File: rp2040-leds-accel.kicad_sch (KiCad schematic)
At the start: 9 parts, among them J1 USB_C_Receptacle_USB2.0_16P, U1 AMS1117-3.3, U2 AMS1117-5.0

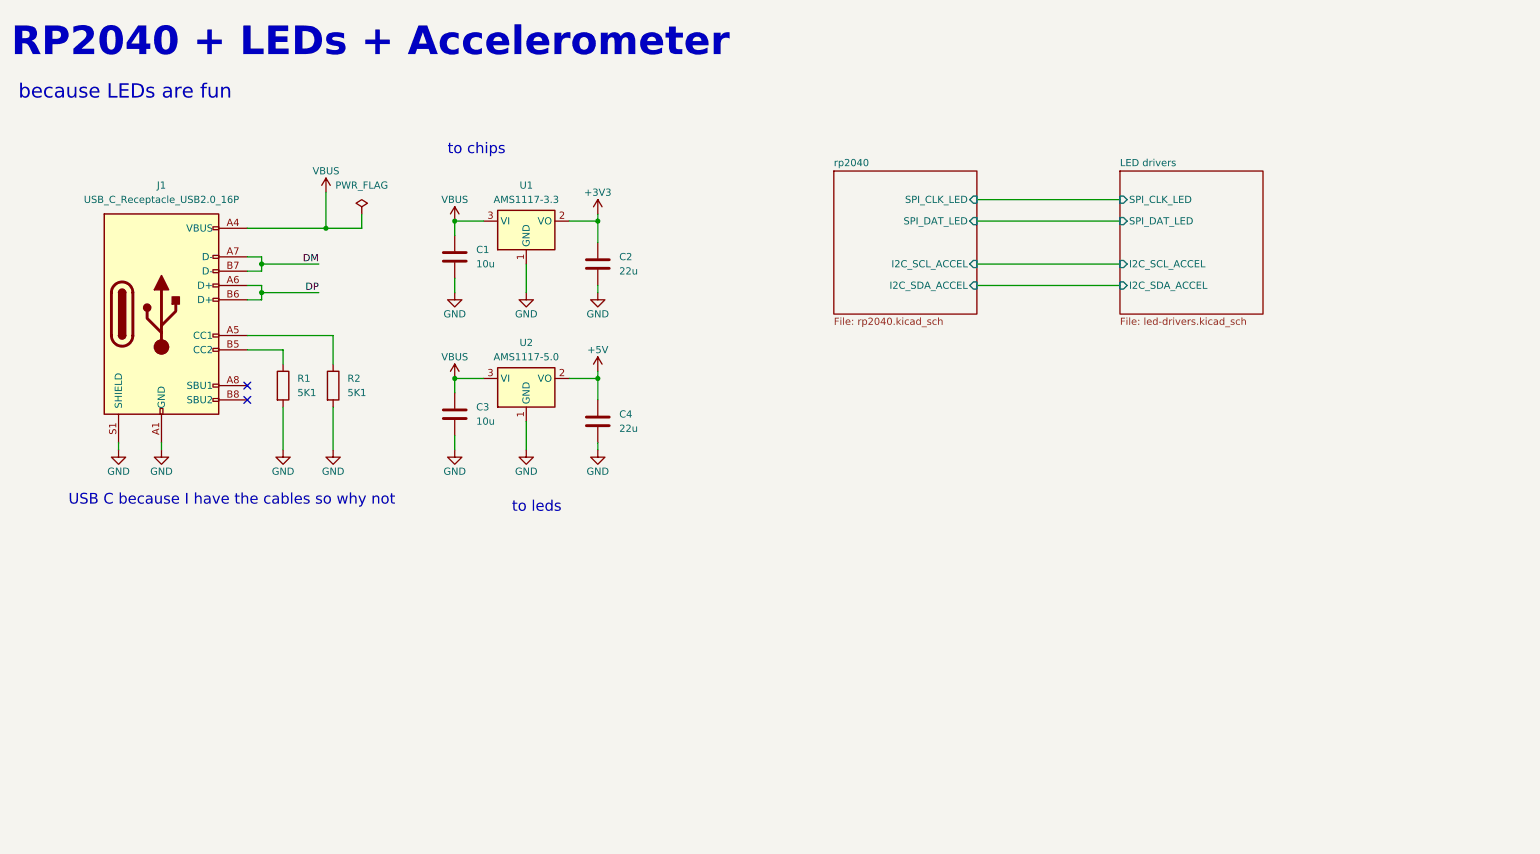
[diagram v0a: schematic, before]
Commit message: Added part numbers, footprints and improved formatting
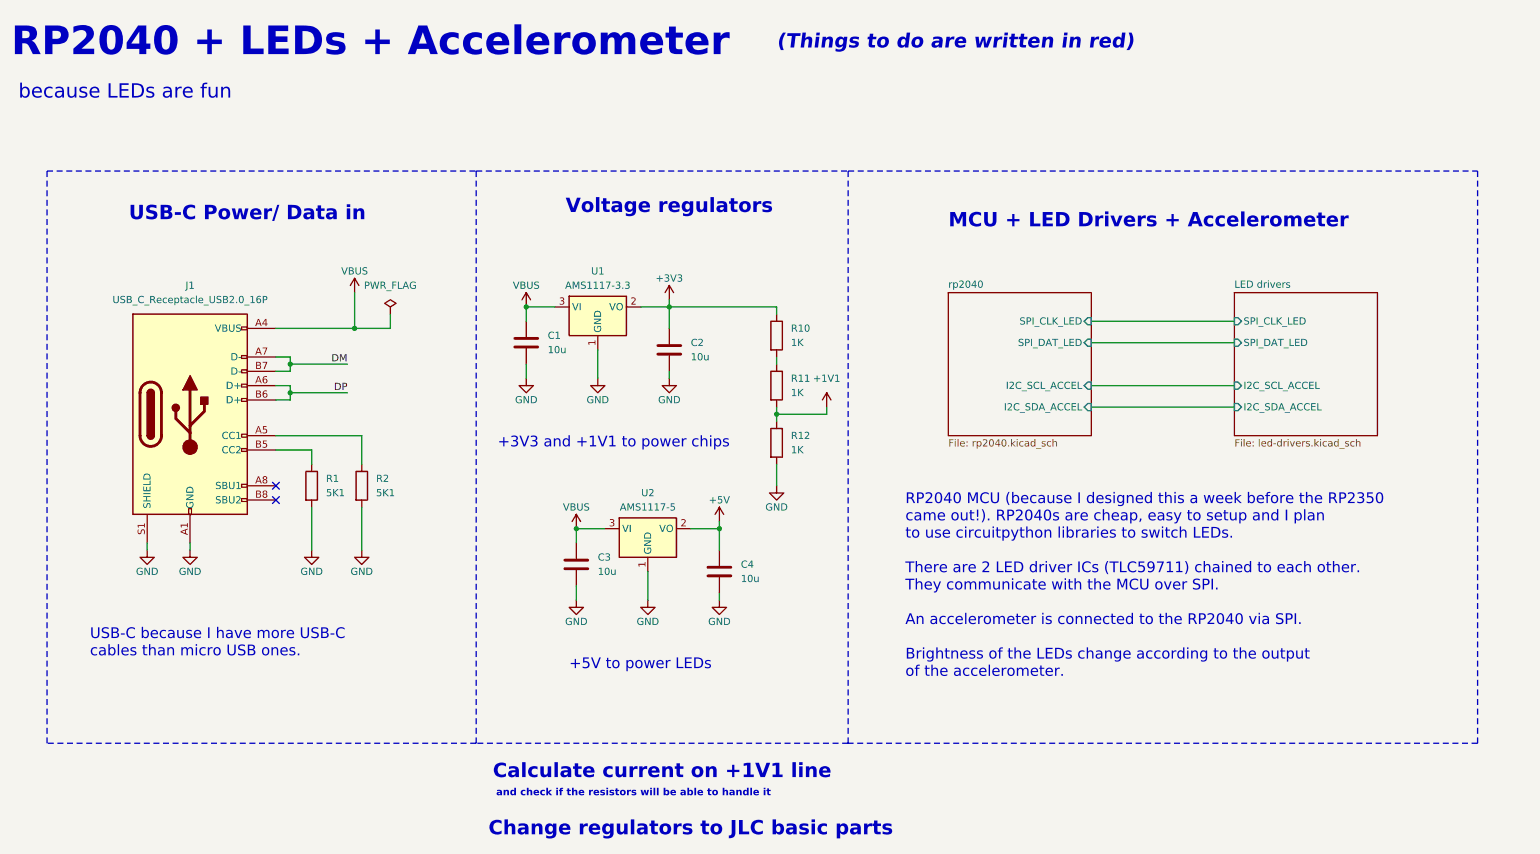
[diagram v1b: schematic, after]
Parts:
- removed C3: 10u, symbol Device:C
- added C3: 10u, Capacitor_SMD:C_0603_1608Metric, symbol jellybeans:C-0603-10u-25V
- added R10, R11, R12: 1K, Resistor_SMD:R_0603_1608Metric, symbol jellybeans:R-0603-1K
- C1: footprint (none) -> Capacitor_SMD:C_0603_1608Metric; symbol Device:C -> jellybeans:C-0603-10u-25V; JLC (none) -> C479655; MFG (none) -> FH (Guangdong Fenghua Advanced Tech); MPN (none) -> 0603X106M250NT
- C2, C4: value 22u -> 10u; footprint (none) -> Capacitor_SMD:C_0805_2012Metric; JLC (none) -> C15850; MFG (none) -> Samsung Electro-Mechanics; MPN (none) -> CL21A106KAYNNNE
- R2: footprint Resistor_SMD:R_0201_0603Metric -> Resistor_SMD:R_0603_1608Metric
- U1: symbol Regulator_Linear:AMS1117-3.3_1 -> suchi_chips:AMS1117-3.3; MPN AMS1117-3.3V -> AMS1117-3.3V
- U2: value AMS1117-5.0 -> AMS1117-5; symbol Regulator_Linear:AMS1117-5.0 -> suchi_chips:AMS1117-5V; JLC (none) -> C6187; MFG (none) -> Advanced Monolithic Systems; MPN (none) -> AMS1117-3.3V
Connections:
- net +3V3: now also R10.1
- net GND: now also C3.2, R12.2
- net VBUS: now also C3.1
- new net: R10.2, R11.1
- new net +1V1: R11.2, R12.1
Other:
- note added: "(Things to do are written in red)"
- note added: "+3V3 and +1V1 to power chips"
- note added: "+5V to power LEDs"
- note added: "Calculate current on +1V1 line"
- note added: "Change regulators to JLC basic parts"
- note added: "MCU + LED Drivers + Accelerometer"
- note added: "RP2040 MCU (because I designed this a week before the RP2350 came out!). RP2040s are cheap, easy to setup and I plan to use circuitpython libraries to switch LEDs. There are 2 LED driver ICs (TLC59711) chained to each other. They communicate with the MCU over SPI. An accelerometer is connected to the RP2040 via SPI. Brightness of the LEDs change according to the output of the accelerometer."
- note added: "USB-C Power/ Data in"
- note added: "USB-C because I have more USB-C cables than micro USB ones."
- note added: "Voltage regulators"
- note added: "and check if the resistors will be able to handle it"
- note removed: "USB C because I have the cables so why not"
- note removed: "to chips"
- note removed: "to leds"
- moved on the sheet: C1, C2, C4, J1, R1, R2, U1, U2
